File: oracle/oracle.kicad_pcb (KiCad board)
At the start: 2 copper layers, 81 x 120.5 mm, 104 parts, among them J1 I2C multiplexer, J10 EXT_PF5, J2 LCD RGB LED, J3 USB-C U-N, J4 USB-C U-S, J5 Banana connector pads, J6 EXT_AREF, J8 BAT, J9 EXT_PE6, Q1 AO3407A, Q2 SS8050, Q3 SS8050, Q4 AO3407A, SW1 12mmx12mm, SW10 12mmx12mm, SW11 12mmx12mm, SW12 12mmx12mm, SW13 12mmx12mm, SW14 12mmx12mm, SW15 12mmx12mm, SW16 12mmx12mm, SW17 12mmx12mm, SW18 12mmx12mm, SW19 12mmx12mm, SW2 12mmx12mm, SW20 12mmx12mm, SW3 12mmx12mm, SW4 12mmx12mm, SW5 12mmx12mm, SW6 12mmx12mm, SW7 12mmx12mm, SW8 12mmx12mm, SW9 12mmx12mm, U1 ATmega32U4-A, U2 WeMos_D1_mini, U5 NE5532, U6 CHG_MOD, Y1 16MHz

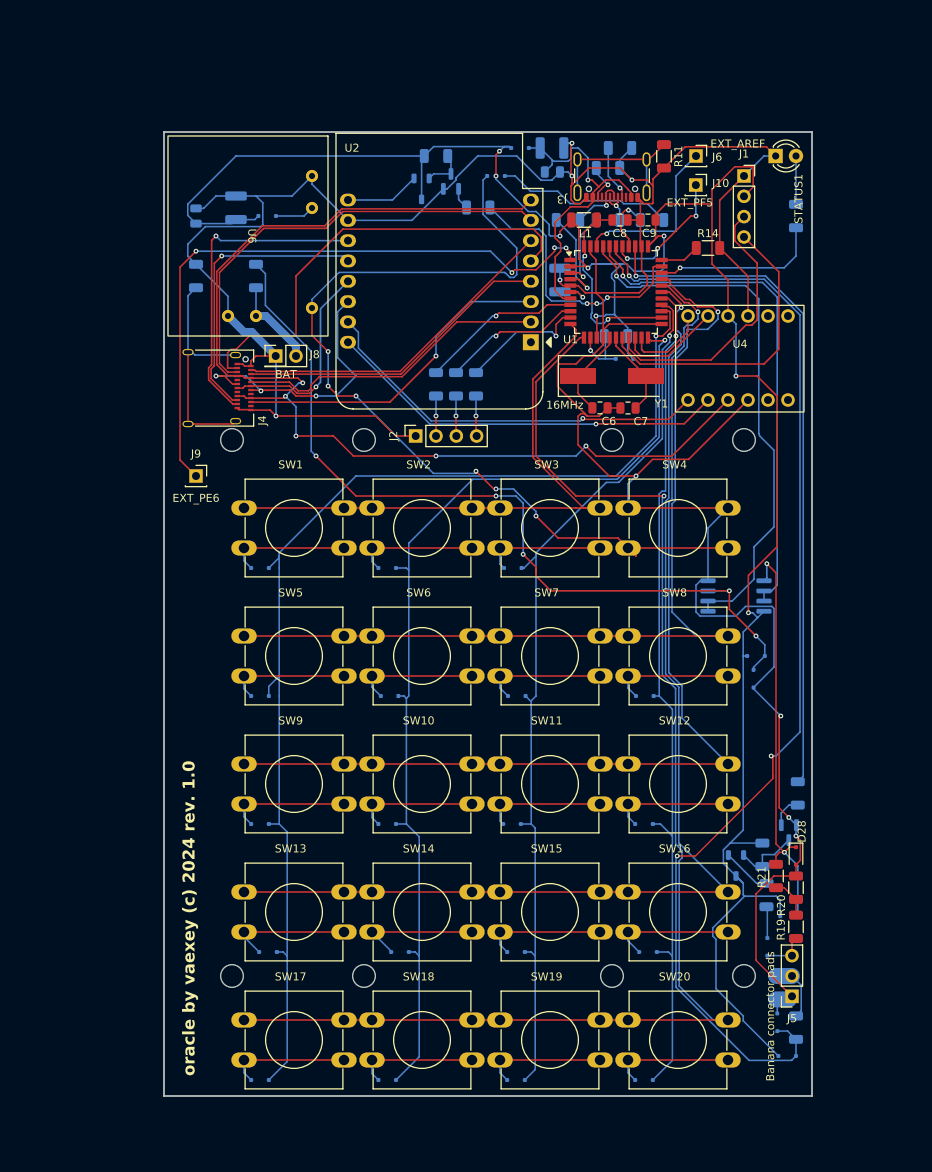
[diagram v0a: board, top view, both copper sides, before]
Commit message: add n_core firmware add e_core firmware stub update PCB
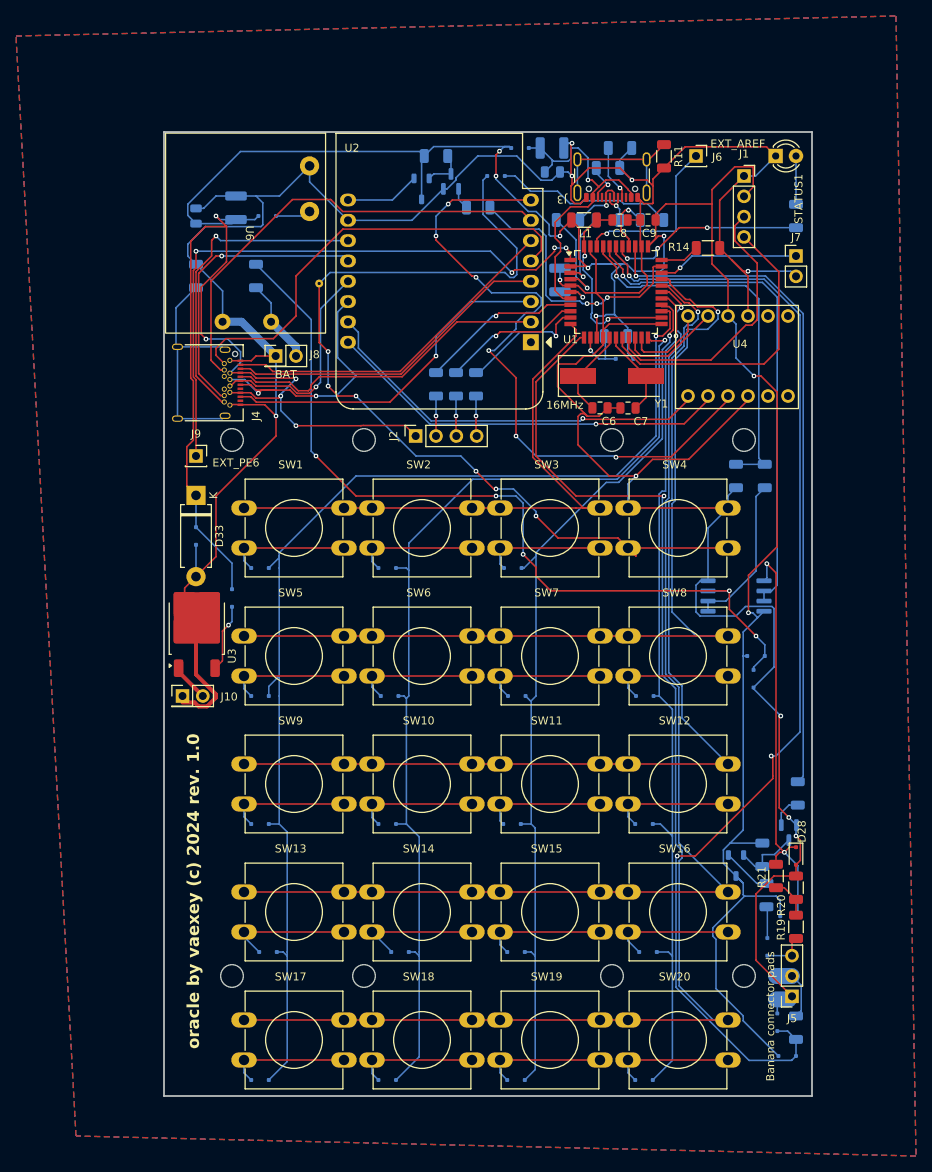
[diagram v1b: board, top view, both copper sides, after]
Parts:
- added D32: 1N4148WS, Diode_SMD:D_SOD-323F, B.Cu at (-2.50, 50.0)
- added D33: 5V1, Diode_THT:D_DO-15_P10.16mm_Horizontal, F.Cu at (-2.50, 44.9)
- added D8: BAT760, Diode_SMD:D_SOD-323F, B.Cu at (2.00, 57.8)
- added J7: BUZZER, Connector_PinHeader_2.54mm:PinHeader_1x02_P2.54mm_Vertical, F.Cu at (72.5, 15.0)
- added R12: 10k, Resistor_SMD:R_1206_3216Metric, B.Cu at (68.6, 42.5)
- added R26: 1k, Resistor_SMD:R_1206_3216Metric, B.Cu at (65.0, 42.5)
- added U3: L7805, Package_TO_SOT_SMD:TO-252-2, F.Cu at (-2.40, 61.5)
- J10: value EXT_PF5 -> EXT_PWR; footprint Connector_PinSocket_2.54mm:PinSocket_1x01_P2.54mm_Vertical -> Connector_PinHeader_2.54mm:PinHeader_2x01_P2.54mm_Vertical
- J4: footprint Connector_USB:USB_C_Receptacle_Amphenol_12401610E4-2A -> Connector_USB:USB_C_Receptacle_Amphenol_12401548E4-2A
- moved J10 90.5 mm to (-4.19, 70.0)
- moved U6 16.1 mm to (13.7, -0.36)
- moved J9 2.50 mm to (-2.50, 40.0)
- moved J4 1.47 mm to (-1.97, 30.8)
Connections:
- J10 pad 1: EXT_PF5 -> GND
- J2 pad 1: GND -> +5V
- J4 pad A4: +3.3V -> +5V
- J4 pad A9: +3.3V -> +5V
- J4 pad B4: +3.3V -> +5V
- J4 pad B9: +3.3V -> +5V
- U1 pad 31: LED_STATUS -> BUZZER
- U1 pad 38: EXT_PF5 -> LED_STATUS
- U5 pad 1: ADC_BAT -> Net-(U5A--)
- U5 pad 2: ADC_BAT -> Net-(U5A--)
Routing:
- net +5V: track 287.5 -> 405.5 mm, vias 8 -> 13
- net +3.3V: track 140.9 -> 85.4 mm, vias 5 -> 6
- net GND: track 407.5 -> 452.9 mm, vias 9 -> 10
- net ADC_BAT: track 68.6 -> 48.2 mm
- net Net-(U5A--): track 0.00 -> 19.7 mm
- net BUZZER: track 0.00 -> 17.7 mm, vias 0 -> 1
- net EXT_PF5: track 17.0 -> 0.00 mm, vias 3 -> 0
- net Net-(D8-A): track 0.00 -> 8.55 mm, vias 0 -> 1
- net Net-(J10-Pin_2): track 0.00 -> 4.73 mm
- net EXT_PE6: track 80.4 -> 76.5 mm
- net LED_STATUS: track 21.2 -> 25.1 mm, vias 1 -> 3
- net ESP_MOSI: track 41.8 -> 43.4 mm
- net ESP_SCK: track 39.8 -> 41.4 mm
- net ESP_A0: track 39.2 -> 40.8 mm
- net ESP_S0: track 41.7 -> 43.3 mm
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- added copper zone on B.Cu, net GND
- added copper zone on F.Cu, net GND
